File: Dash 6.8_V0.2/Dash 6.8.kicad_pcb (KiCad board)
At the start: 2 copper layers, 156 x 66 mm, 151 parts, among them J1 USB_B_Mini, J2 Conn_01x04, J3 20279-001E-03, J4 Conn_01x40_MountingPin, J5 776262-1, J6 Conn_01x04, Q1 DMP3013SFV-7, SW1 SW_Push, SW2 SW_Push, U1 REF3333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

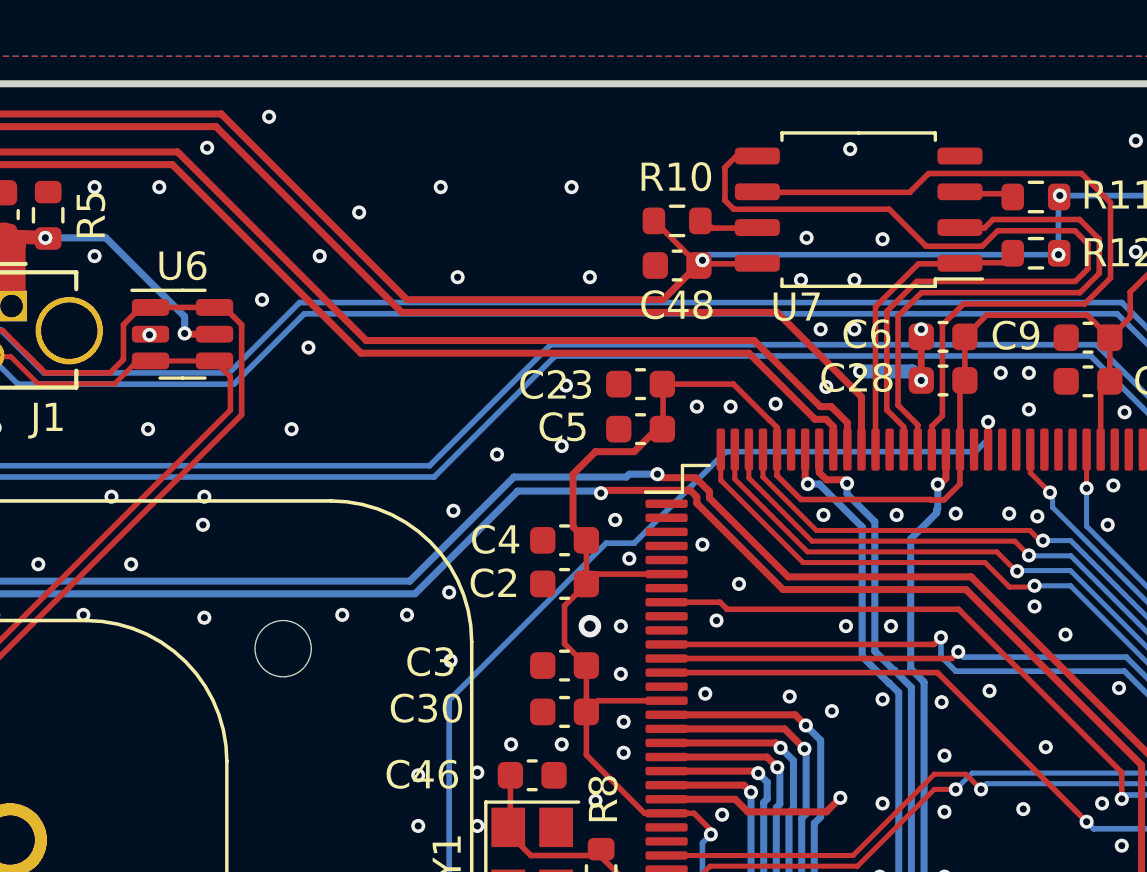
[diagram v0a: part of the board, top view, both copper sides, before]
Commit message: исправление платы V02
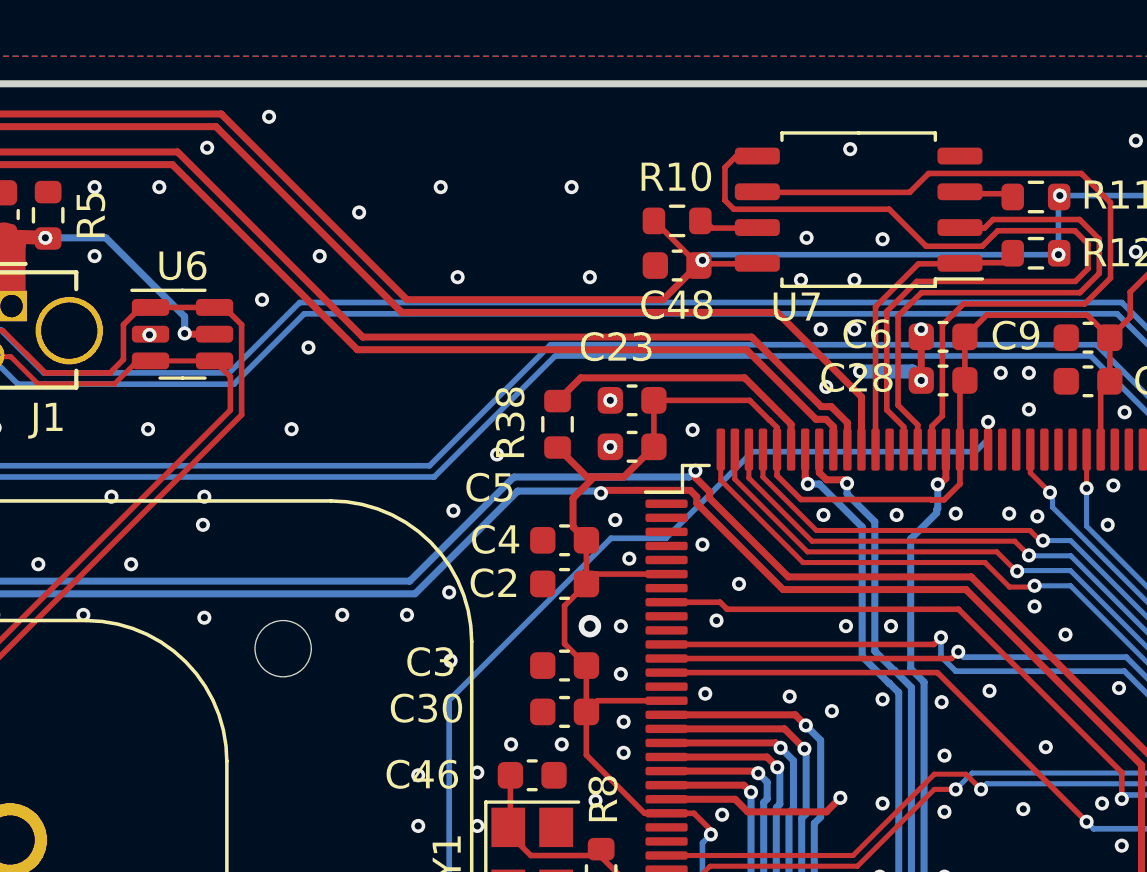
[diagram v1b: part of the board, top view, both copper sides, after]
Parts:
- added R38: 10k, Resistor_SMD:R_0603_1608Metric, F.Cu at (178.4, 89.2)
- moved C5 0.70 mm to (181.1, 90.0)
- moved C23 0.65 mm to (181.1, 88.4)
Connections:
- R31 pad 2: Net-(U12--) -> GND
- U12 pad 1: Net-(U12--) -> GND
- U12 pad 4: Net-(U12--) -> GND
- U4 pad 171: unconnected-(U4-PDR_ON-Pad171) -> Net-(U4-PDR_ON)
- U4 pad 48: unconnected-(U4-BYPASS_REG-Pad48) -> GND
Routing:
- net Net-(U4-PDR_ON): track 0.00 -> 10.2 mm
- net GND: track 89.0 -> 94.6 mm, vias 474 -> 472
- net Net-(U12--): track 5.58 -> 0.00 mm
